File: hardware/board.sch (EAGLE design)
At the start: 130 parts, among them CON2 USB-FPGA-2THT, IC1 THS3062, IC2 AD80XX, U1 AD9215BRUZ, X1 BU-SMA-V

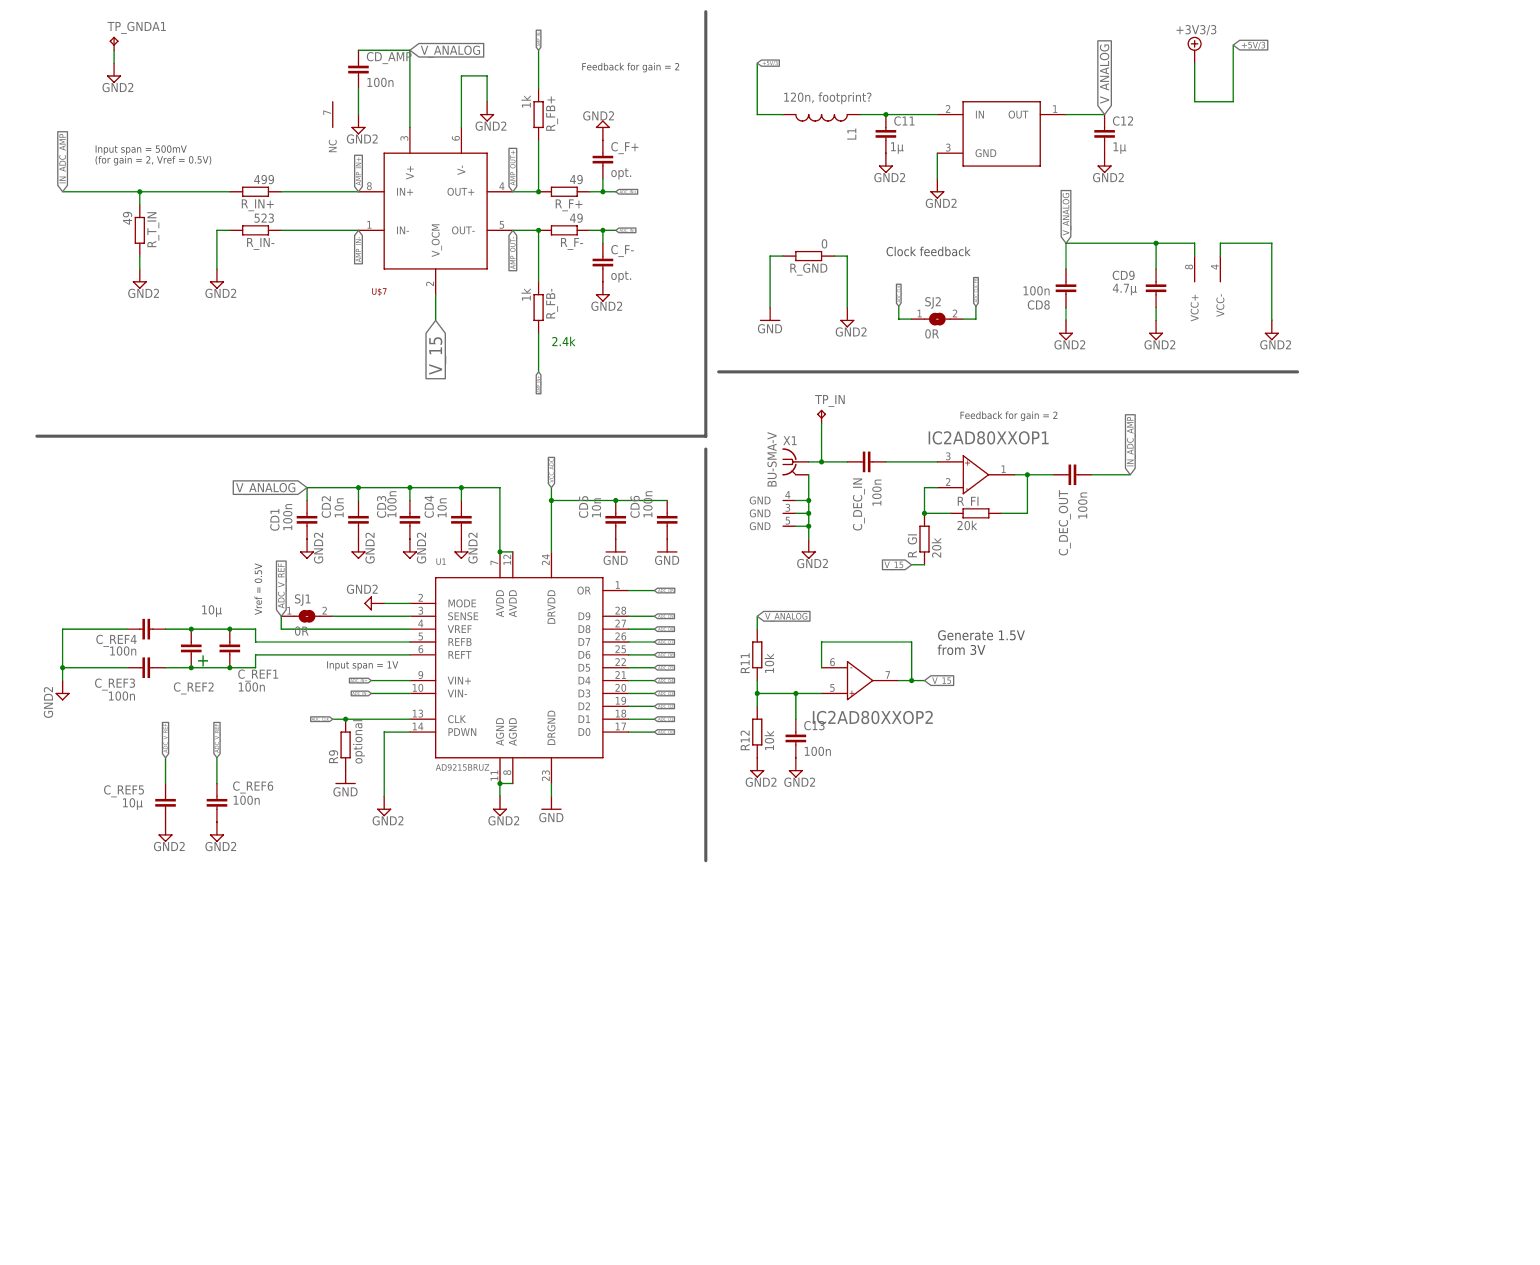
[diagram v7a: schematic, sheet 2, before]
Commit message: Placed ADC components Changed ADC VR
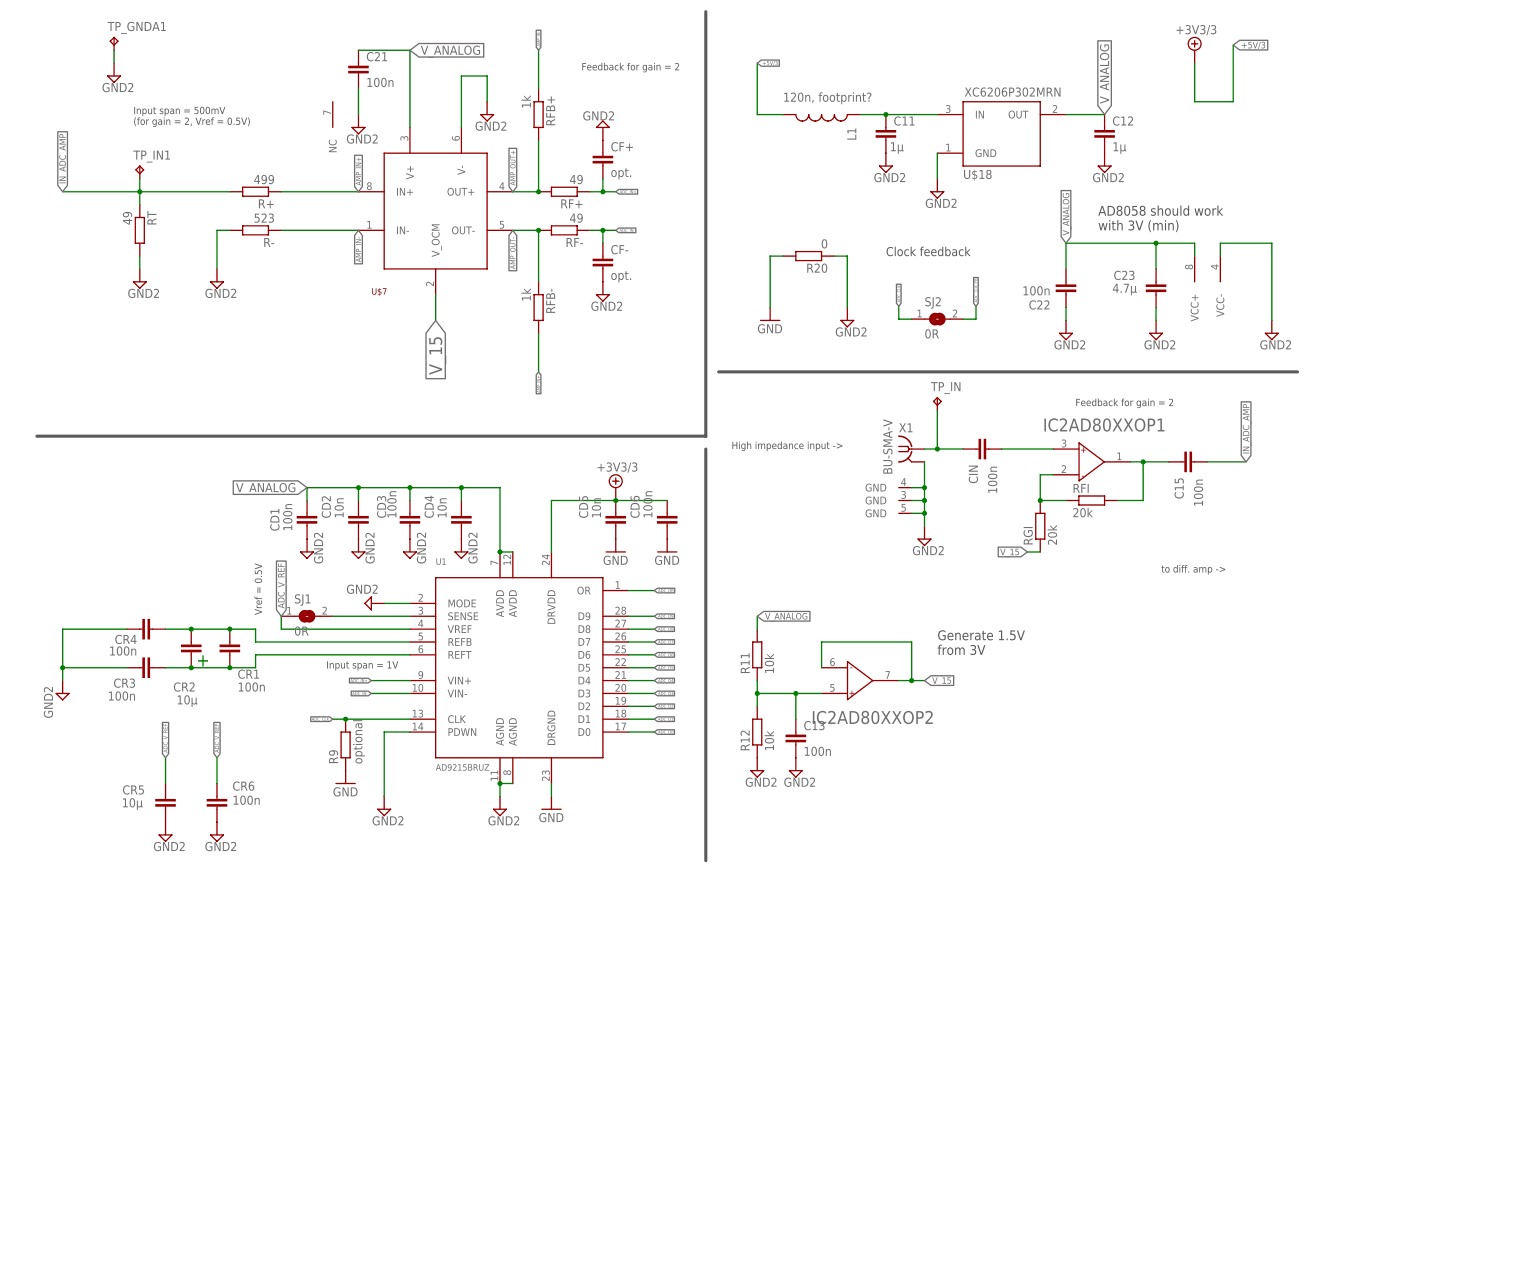
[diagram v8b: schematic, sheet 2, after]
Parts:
- removed CD9: 4.7µ, rcl:C-EUC1206
- removed C_DEC_IN, C_DEC_OUT: 100n, rcl:C-EUC0603
- removed C_REF2, C_REF5: 10µ, rcl:C-EUC1206
- removed R_FI, R_GI: 20k, rcl:R-EU_R0603
- added C15, CIN: 100n, rcl:C-EUC0603
- added C23: 4.7µ, rcl:C-EUC0805K
- added CR2, CR5: 10µ, rcl:C-EUC0805K
- added RFI, RGI: 20k, rcl:R-EU_R0603
- added TP_IN1: TPPAD1-13, testpad:TPPAD1-13
- C11, C12: device rcl:C-EUC1206 -> rcl:C-EUC0805K
- U$18: value TS5204 -> XC6206P302MRN; device ts5204:TS5204 -> XC6206:XC6206
- renumbered CD8 to C22, CD_AMP to C21, C_F+ to CF+, C_F- to CF-, C_REF1 to CR1, C_REF3 to CR3, C_REF4 to CR4, C_REF6 to CR6, R_F+ to RF+, R_F- to RF-, R_FB+ to RFB+, R_FB- to RFB-, R_GND to R20, R_IN+ to R+, R_IN- to R-, R_T_IN to RT
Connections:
- removed net VCC_ADC: CD5.1, CD6.1, U1.DRVDD
- net +5V/3: now also CD5.1, CD6.1, U1.DRVDD
- net ADC_V_REF: now also CR5.2; no longer C_REF5.2
- net GND2: now also C23.1, CR5.1; no longer CD9.1, C_REF5.1
- net IN_ADC_AMP: now also C15.2, TP_IN1.TP; no longer C_DEC_OUT.2
- net N$21: now also C15.1, RFI.2; no longer C_DEC_OUT.1, R_FI.2
- net N$25: now also RFI.1, RGI.2; no longer R_FI.1, R_GI.2
- net N$5: now also CR2.2; no longer C_REF2.2
- net N$6: now also CR2.1; no longer C_REF2.1
- net N$8: now also CIN.1; no longer C_DEC_IN.1
- net N$9: now also CIN.2; no longer C_DEC_IN.2
- net V_15: now also RGI.1; no longer R_GI.1
- net V_ANALOG: now also C23.2; no longer CD9.2
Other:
- note added: "AD8058 should work with 3V (min)"
- note added: "High impedance input ->"
- note added: "to diff. amp ->"
- note removed: "2.4k"
- note removed: "CHANGE: XC6206P302MR 3V LDO, 90 deg rotated or other 3V"
- note removed: "Check if 3V ok?"
- moved on the sheet: IC2AD80XXOP1, TP_IN, X1
